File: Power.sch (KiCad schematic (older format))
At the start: 35 parts, among them T5 Test_Point, T6 Test_Point, T7 Test_Point, U4 MP4570GF, U5 AP65251, U6 AZ1117-3.3

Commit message: Switch to new kicad footprint library
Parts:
- C10, C11: footprint Capacitors_SMD:C_0805 -> Capacitor_SMD:C_0603_1608Metric
- C13, C15, C16, C17, C19, C7: footprint Capacitors_SMD:C_0603 -> Capacitor_SMD:C_0603_1608Metric
- R10, R11, R12, R3, R4, R5, R6, R7: footprint Resistors_SMD:R_0603 -> Resistor_SMD:R_0603_1608Metric
- U4: footprint Housings_SSOP:HTSSOP-20-1EP_4.4x6.5mm_Pitch0.65mm_ThermalPad -> Package_SO:HTSSOP-20-1EP_4.4x6.5mm_P0.65mm_EP3.4x6.5mm_ThermalVias
- U6: footprint TO_SOT_Packages_SMD:SOT-223-3_TabPin2 -> Package_TO_SOT_SMD:SOT-223-3_TabPin2
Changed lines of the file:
@@
 F 0 "U6" H 9525 1425 50  0000 C CNN
 F 1 "AZ1117-3.3" H 9150 1800 50  0000 L CNN
-F 2 "TO_SOT_Packages_SMD:SOT-223-3_TabPin2" H 9375 1925 50  0001 C CIN
+F 2 "Package_TO_SOT_SMD:SOT-223-3_TabPin2" H 9375 1925 50  0001 C CIN
 F 3 "" H 9375 1675 50  0001 C CNN
 F 4 "https://www.digikey.com/product-detail/en/diodes-incorporated/AZ1117CH-3.3TRG1/AZ1117CH-3.3TRG1DICT-ND/4505206" H 9375 1675 50  0001 C CNN "Buy"
@@
 F 0 "R10" V 4855 1525 50  0000 C CNN
 F 1 "100k" V 4775 1525 50  0000 C CNN
-F 2 "Resistors_SMD:R_0603" V 4705 1525 50  0001 C CNN
+F 2 "Resistor_SMD:R_0603_1608Metric" V 4705 1525 50  0001 C CNN
 F 3 "" H 4775 1525 50  0001 C CNN
 F 4 "https://www.digikey.com/product-detail/en/yageo/RC0603JR-10100KL/YAG2294CT-ND/5252408" V 4775 1525 50  0001 C CNN "Buy"
@@
 F 0 "R11" V 6505 1825 50  0000 C CNN
 F 1 "73k2" V 6425 1825 50  0000 C CNN
-F 2 "Resistors_SMD:R_0603" V 6355 1825 50  0001 C CNN
+F 2 "Resistor_SMD:R_0603_1608Metric" V 6355 1825 50  0001 C CNN
 F 3 "" H 6425 1825 50  0001 C CNN
 F 4 "https://www.digikey.com/product-detail/en/yageo/RC0603FR-0773K2L/311-73.2KHRCT-ND/730321" V 6425 1825 50  0001 C CNN "Buy"
@@
 F 0 "R12" V 6505 2225 50  0000 C CNN
 F 1 "10k" V 6425 2225 50  0000 C CNN
-F 2 "Resistors_SMD:R_0603" V 6355 2225 50  0001 C CNN
+F 2 "Resistor_SMD:R_0603_1608Metric" V 6355 2225 50  0001 C CNN
 F 3 "" H 6425 2225 50  0001 C CNN
 F 4 "https://www.digikey.com/product-detail/en/yageo/RC0603FR-0710KL/311-10.0KHRCT-ND/729827" V 6425 2225 50  0001 C CNN "Buy"
@@
 F 0 "C16" H 5875 1425 50  0000 L CNN
 F 1 "100nF" H 5875 1625 50  0000 L CNN
-F 2 "Capacitors_SMD:C_0603" H 5863 1375 50  0001 C CNN
+F 2 "Capacitor_SMD:C_0603_1608Metric" H 5863 1375 50  0001 C CNN
 F 3 "" H 5825 1525 50  0001 C CNN
 F 4 "https://www.digikey.com/product-detail/en/kemet/C0603C104K3RACTU/399-1281-1-ND/416057" H 5825 1525 50  0001 C CNN "Buy"
@@
 F 0 "C17" H 6700 1925 50  0000 L CNN
 F 1 "30pF" H 6700 1725 50  0000 L CNN
-F 2 "Capacitors_SMD:C_0603" H 6713 1675 50  0001 C CNN
+F 2 "Capacitor_SMD:C_0603_1608Metric" H 6713 1675 50  0001 C CNN
 F 3 "" H 6675 1825 50  0001 C CNN
 F 4 "https://www.digikey.com/product-detail/en/samsung-electro-mechanics/CL10C300JB8NNNC/1276-1021-1-ND/3889107" H 6675 1825 50  0001 C CNN "Buy"
@@
 F 0 "C11" H 2160 1820 50  0000 L CNN
 F 1 "100nF" H 2150 1675 50  0000 L CNN
-F 2 "Capacitors_SMD:C_0805" H 2150 1750 50  0001 C CNN
+F 2 "Capacitor_SMD:C_0603_1608Metric" H 2150 1750 50  0001 C CNN
 F 3 "" H 2150 1750 50  0001 C CNN
 F 4 "https://www.digikey.com/product-detail/en/samsung-electro-mechanics/CL21B104KCFWPNE/1276-6733-1-ND/5961592" H 2150 1750 50  0001 C CNN "Buy"
@@
 F 0 "R5" V 1030 2800 50  0000 C CNN
 F 1 "73k2" V 950 2800 50  0000 C CNN
-F 2 "Resistors_SMD:R_0603" V 880 2800 50  0001 C CNN
+F 2 "Resistor_SMD:R_0603_1608Metric" V 880 2800 50  0001 C CNN
 F 3 "" H 950 2800 50  0001 C CNN
 F 4 "https://www.digikey.com/product-detail/en/yageo/RC0603FR-0773K2L/311-73.2KHRCT-ND/730321" V 950 2800 50  0001 C CNN "Buy"
@@
 F 0 "C10" H 1760 1170 50  0000 L CNN
 F 1 "100nF" H 1750 1025 50  0000 L CNN
-F 2 "Capacitors_SMD:C_0805" H 1750 1100 50  0001 C CNN
+F 2 "Capacitor_SMD:C_0603_1608Metric" H 1750 1100 50  0001 C CNN
 F 3 "" H 1750 1100 50  0001 C CNN
 F 4 "https://www.digikey.com/product-detail/en/samsung-electro-mechanics/CL21B104KCFWPNE/1276-6733-1-ND/5961592" H 1750 1100 50  0001 C CNN "Buy"
@@
 F 0 "R4" V 830 1600 50  0000 C CNN
 F 1 "1M" V 750 1600 50  0000 C CNN
-F 2 "Resistors_SMD:R_0603" V 680 1600 50  0001 C CNN
+F 2 "Resistor_SMD:R_0603_1608Metric" V 680 1600 50  0001 C CNN
 F 3 "" H 750 1600 50  0001 C CNN
 F 4 "https://www.digikey.com/product-detail/en/yageo/RC0603JR-071ML/311-1.0MGRCT-ND/729625" V 750 1600 50  0001 C CNN "Buy"
@@
 F 0 "R6" V 2880 2100 50  0000 C CNN
 F 1 "10k" V 2800 2100 50  0000 C CNN
-F 2 "Resistors_SMD:R_0603" V 2730 2100 50  0001 C CNN
+F 2 "Resistor_SMD:R_0603_1608Metric" V 2730 2100 50  0001 C CNN
 F 3 "" H 2800 2100 50  0001 C CNN
 F 4 "https://www.digikey.com/product-detail/en/yageo/RC0603FR-0710KL/311-10.0KHRCT-ND/729827" V 2800 2100 50  0001 C CNN "Buy"
@@
 F 0 "R7" V 2880 2500 50  0000 C CNN
 F 1 "910" V 2800 2500 50  0000 C CNN
-F 2 "Resistors_SMD:R_0603" V 2730 2500 50  0001 C CNN
+F 2 "Resistor_SMD:R_0603_1608Metric" V 2730 2500 50  0001 C CNN
 F 3 "" H 2800 2500 50  0001 C CNN
 F 4 "https://www.digikey.com/product-detail/en/yageo/RC0603FR-07909RL/311-909HRCT-ND/730372" V 2800 2500 50  0001 C CNN "Buy"
@@
 F 0 "C13" H 3785 2170 50  0000 L CNN
 F 1 "100nF" H 3775 2025 50  0000 L CNN
-F 2 "Capacitors_SMD:C_0603" H 3775 2100 50  0001 C CNN
+F 2 "Capacitor_SMD:C_0603_1608Metric" H 3775 2100 50  0001 C CNN
 F 3 "" H 3775 2100 50  0001 C CNN
 F 4 "https://www.digikey.com/product-detail/en/kemet/C0603C104K3RACTU/399-1281-1-ND/416057" H 3775 2100 50  0001 C CNN "Buy"
@@
 F 0 "R3" V 780 2600 50  0000 C CNN
 F 1 "30k9" V 700 2600 50  0000 C CNN
-F 2 "Resistors_SMD:R_0603" V 630 2600 50  0001 C CNN
+F 2 "Resistor_SMD:R_0603_1608Metric" V 630 2600 50  0001 C CNN
 F 3 "" H 700 2600 50  0001 C CNN
 F 4 "https://www.digikey.com/product-detail/en/yageo/RC0603FR-0730K9L/311-30.9KHRCT-ND/730091" V 700 2600 50  0001 C CNN "Buy"
@@
 F 0 "C7" H 710 2970 50  0000 L CNN
 F 1 "22nF" H 710 2820 50  0000 L CNN
-F 2 "Capacitors_SMD:C_0603" H 700 2900 50  0001 C CNN
+F 2 "Capacitor_SMD:C_0603_1608Metric" H 700 2900 50  0001 C CNN
 F 3 "" H 700 2900 50  0001 C CNN
 F 4 "https://www.digikey.com/product-detail/en/kemet/C0603C223K1RACTU/399-3476-1-ND/754769" H 700 2900 50  0001 C CNN "Buy"
@@
 F 0 "C15" H 4510 1620 50  0000 L CNN
 F 1 "100nF" H 4500 1475 50  0000 L CNN
-F 2 "Capacitors_SMD:C_0603" H 4500 1550 50  0001 C CNN
+F 2 "Capacitor_SMD:C_0603_1608Metric" H 4500 1550 50  0001 C CNN
 F 3 "" H 4500 1550 50  0001 C CNN
 F 4 "https://www.digikey.com/product-detail/en/kemet/C0603C104K3RACTU/399-1281-1-ND/416057" H 4500 1550 50  0001 C CNN "Buy"
@@
 F 0 "C19" H 7450 1925 50  0000 L CNN
 F 1 "100nF" H 7450 1725 50  0000 L CNN
-F 2 "Capacitors_SMD:C_0603" H 7463 1675 50  0001 C CNN
+F 2 "Capacitor_SMD:C_0603_1608Metric" H 7463 1675 50  0001 C CNN
 F 3 "" H 7425 1825 50  0001 C CNN
 F 4 "https://www.digikey.com/product-detail/en/kemet/C0603C104K3RACTU/399-1281-1-ND/416057" H 7425 1825 50  0001 C CNN "Buy"
@@
 F 0 "U4" H 1950 2100 60  0000 C CNN
 F 1 "MP4570GF" H 1550 2900 60  0000 C CNN
-F 2 "Housings_SSOP:HTSSOP-20-1EP_4.4x6.5mm_Pitch0.65mm_ThermalPad" H 400 2900 60  0001 C CNN
+F 2 "Package_SO:HTSSOP-20-1EP_4.4x6.5mm_P0.65mm_EP3.4x6.5mm_ThermalVias" H 400 2900 60  0001 C CNN
 F 3 "" H 400 2900 60  0001 C CNN
 F 4 "https://www.mouser.de/ProductDetail/Monolithic-Power-Systems-MPS/MP4570GF-Z?qs=sGAEpiMZZMtitjHzVIkrqU99irDpZcy8vQddg2chZTNyXKTpjLDESQ%3d%3d" H 1550 2500 50  0001 C CNN "Buy"
@@
 $EndComp
 $Comp
-L power:PWR_FLAG #FLG?
+L power:PWR_FLAG #FLG0101
 U 1 1 5ABB1D1C
 P 10375 1625
-F 0 "#FLG?" H 10375 1700 50  0001 C CNN
+F 0 "#FLG0101" H 10375 1700 50  0001 C CNN
 F 1 "PWR_FLAG" H 10375 1775 50  0000 C CNN
 F 2 "" H 10375 1625 50  0001 C CNN

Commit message: Add custom footprint for TSOT-26
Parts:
- U5: footprint (none) -> erleuchtung-footprints:TSOT-26
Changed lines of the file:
@@
 F 0 "U5" H 5025 1725 60  0000 C CNN
 F 1 "AP65251" H 5375 2575 60  0000 C CNN
-F 2 "" H 5275 1925 60  0001 C CNN
+F 2 "erleuchtung-footprints:TSOT-26" H 5275 1925 60  0001 C CNN
 F 3 "https://www.diodes.com/assets/Datasheets/AP65111A.pdf" H 5275 1925 60  0001 C CNN
 F 4 "https://www.digikey.com/product-detail/en/diodes-incorporated/AP65251WU-7/AP65251WU-7DICT-ND/7915274" H 5275 1925 50  0001 C CNN "Buy"

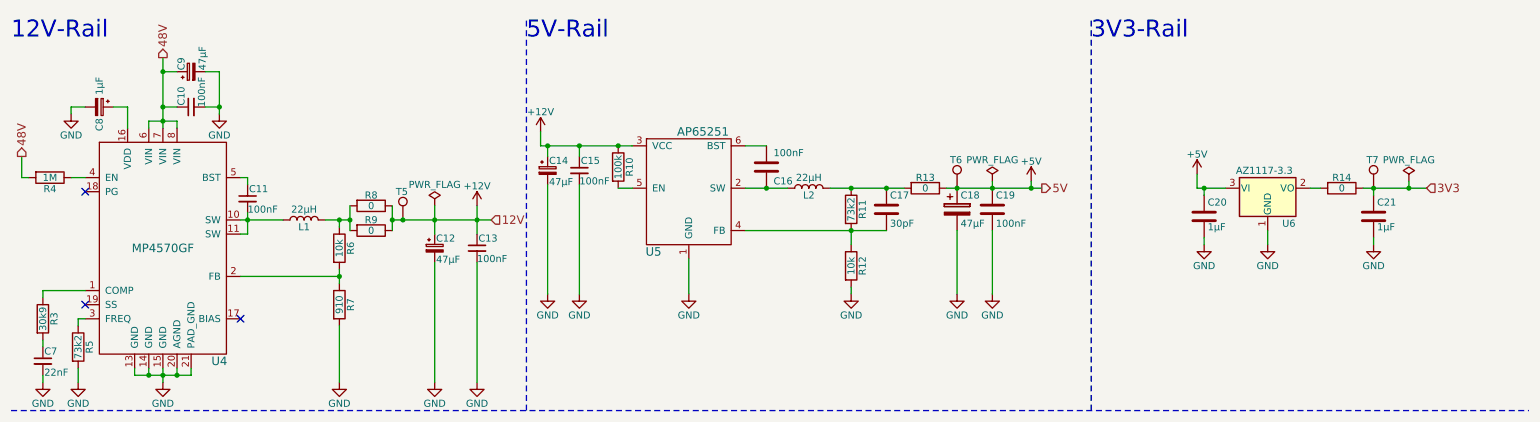
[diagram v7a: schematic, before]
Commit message: Replaced the 0-Resistors with Solder-Brigdes
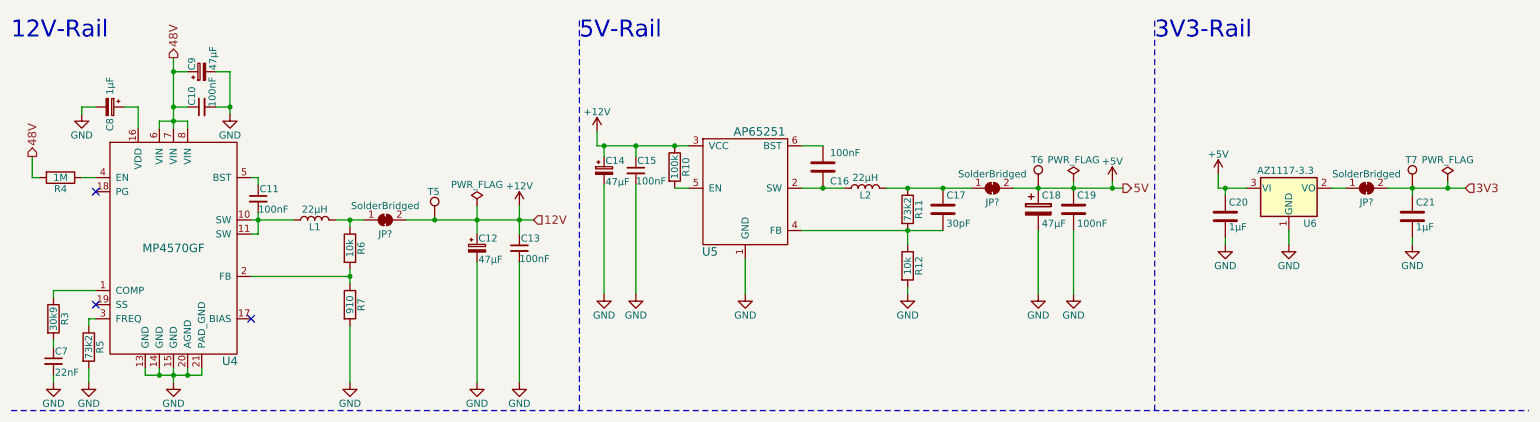
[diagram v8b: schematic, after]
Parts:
- removed R13, R14, R8, R9: 0, symbol Device:R
- added JP? (x3): SolderBridged, symbol Jumper:SolderJumper_2_Bridged
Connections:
- net +12V: now also JP?.2 (B)
- net +5V: now also JP?.2 (B)
- net 3V3: now also JP?.2 (B)
- net at U6.2 (VO): now also JP?.1 (A)
- net at C17.1, L2.2, R11.1: now also JP?.1 (A)
- net at L1.2, R6.1: now also JP?.1 (A)
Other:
- moved on the sheet: C10, C11, C12, C13, C14, C15, C16, C17, C18, C19, C20, C21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
